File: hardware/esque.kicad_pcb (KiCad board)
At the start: 2 copper layers, 54.6 x 39.7 mm, 11 parts, among them J2 Conn_01x03_Pin, J3 Conn_01x04_Pin

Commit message: Update two-board hardware design to revision 0.9
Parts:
- removed A1: Arduino_Nano_v2.x, Module:Arduino_Nano
- removed J3: Conn_01x04_Pin, Connector:FanPinHeader_1x04_P2.54mm_Vertical
- added C1: 10pF, Capacitor_SMD:C_1206_3216Metric, B.Cu at (27.0, 40.0)
- added C2: 10pF, Capacitor_SMD:C_1206_3216Metric, B.Cu at (42.0, 36.5)
- added C3: 100nF, Capacitor_SMD:C_1206_3216Metric, B.Cu at (27.9, 30.2)
- added C4: 100nF, Capacitor_SMD:C_1206_3216Metric, B.Cu at (40.5, 31.5)
- added C6: 10uF 16V, Turbimeter:CP_Radial_D5_P2_SingleFace, F.Cu at (47.0, 38.5)
- added J1: SENSOR_LINK_2mm, Turbimeter:StackHeader_1x06_P2mm_Base_SingleFace, F.Cu at (47.3, 24.0)
- added J4: USB_STACK_4_1.27mm, Turbimeter:USB_StackHeader_2x02_P1.27mm_Base_v09, F.Cu at (33.5, 47.0)
- added R4: 10k, Resistor_SMD:R_1206_3216Metric, B.Cu at (45.5, 31.7)
- added U1: MCP6002-E/P, Turbimeter:MCP6002_DIP8_SingleFace, F.Cu at (30.5, 34.4)
- D1: value LED -> BPW34 scatter; footprint LED_THT:LED_D3.0mm_Horizontal_O6.35mm_Z10.0mm -> Turbimeter:BPW34_Holder_v08; moved to F.Cu
- D2: value LED -> BPW34 reference; footprint LED_THT:LED_D3.0mm_Horizontal_O6.35mm_Z10.0mm -> Turbimeter:BPW34_Holder_v08; moved to F.Cu
- D3: value LED -> 850 nm IR; footprint LED_THT:LED_D3.0mm_Horizontal_O6.35mm_Z10.0mm -> Turbimeter:LED850_LeadPads_P2.54mm; moved to F.Cu
- J2: value Conn_01x03_Pin -> USB2_CABLE_4_WIRES; footprint Connector_PinHeader_2.54mm:PinHeader_1x03_P2.54mm_Vertical -> Turbimeter:USB_Cable_WireHoles_2x02_P2mm; moved to F.Cu
- R1, R2: value R -> 1M; footprint Resistor_THT:R_Axial_DIN0207_L6.3mm_D2.5mm_P10.16mm_Horizontal -> Resistor_SMD:R_1206_3216Metric
- R3: value R -> 10k; footprint Resistor_THT:R_Axial_DIN0207_L6.3mm_D2.5mm_P10.16mm_Horizontal -> Resistor_SMD:R_1206_3216Metric
- R5, R6: value R -> 220R; footprint Resistor_THT:R_Axial_DIN0207_L6.3mm_D2.5mm_P10.16mm_Horizontal -> Resistor_SMD:R_1206_3216Metric
- moved R6 124.7 mm to (19.0, 29.0), turned to 90 degrees
- moved R5 116.0 mm to (19.0, 34.0)
- moved D2 104.8 mm to (23.0, 29.5), turned to -90 degrees
- moved D1 102.5 mm to (31.5, 30.2)
- moved J2 100.9 mm to (25.7, 43.5), turned to 0 degrees
- moved D3 99.2 mm to (23.5, 25.7), turned to 90 degrees
- moved R1 88.8 mm to (27.0, 35.0), turned to 90 degrees
- moved R2 73.6 mm to (42.0, 34.0)
- moved R3 72.3 mm to (44.5, 27.0), turned to 90 degrees
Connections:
- D1 pad 1: D5 -> /SCATTER_SUM
- D1 pad 2: Net-(D1-A) -> /GND
- D2 pad 1: D4 -> /REFERENCE_SUM
- D2 pad 2: Net-(D2-A) -> /GND
- D3 pad 1: D3 -> /GND
- D3 pad 2: Net-(D3-A) -> /LED_ANODE
- J2 pad 1: GND -> /USB_VBUS
- J2 pad 2: +5V -> /GND
- J2 pad 3: A1 -> /USB_DM
- R1 pad 1: Net-(D3-A) -> /SCATTER_OUT
- R1 pad 2: +3.3V -> /SCATTER_SUM
- R2 pad 1: Net-(D2-A) -> /REFERENCE_OUT
- R2 pad 2: +3.3V -> /REFERENCE_SUM
- R3 pad 1: Net-(D1-A) -> /3V3
- R3 pad 2: +3.3V -> /VREF
- R5 pad 1: A5 -> /LED_DRIVE
- R5 pad 2: +3.3V -> /LED_R1
- R6 pad 1: A4 -> /LED_R1
- R6 pad 2: +3.3V -> /LED_ANODE
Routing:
- net +3.3V: track 88.5 -> 0.00 mm
- net A4: track 43.0 -> 0.00 mm
- net A5: track 33.1 -> 0.00 mm
- net Net-(D1-A): track 28.0 -> 0.00 mm
- net Net-(D2-A): track 23.0 -> 0.00 mm
- net A1: track 18.7 -> 0.00 mm
- net Net-(D3-A): track 17.2 -> 0.00 mm
- net D3: track 13.7 -> 0.00 mm
- net D4: track 11.9 -> 0.00 mm
- net D5: track 11.4 -> 0.00 mm
- net +5V: track 4.38 -> 0.00 mm
- net GND: vias 4 -> 0
- removed copper zone on F.Cu, net GND
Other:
- board size 54.6 x 39.7 mm -> 37.1 x 35.6 mm
- board text added: "44mm circle = enclosure clearance; NOT Edge.Cuts"
- board text added: "B.Cu ONLY — SOLDER SIDE: SMD, ALL JOINTS AND ROUTING"
- board text added: "BOTTOM"
- board text added: "Design: Ing. Alex M. Rivera"
- board text added: "J1: GND / 3V3 / LED / SCATTER / REFERENCE / GND"
- board text added: "J2/J4/J5 USB 1..4: VBUS / GND / D- / D+; CC termination at cable plugs / OTG adapter"
- board text added: "NO F.Cu TRACKS / ZONES; NO VIAS. PAD 1 MARKED SQUARE."
- board text added: "SMD + ALL SOLDER + TRACKS"
- board text added: "THT TOP - SOLDER BELOW"
- board text added: "TOP"
- board text added: "TOP / F.Cu: THROUGH-HOLE COMPONENTS AND MALE HEADERS"
- board text added: "Turbidimeter | floor 1 - sensor / cable entry"
- board text added: "UNROUTED - DO NOT FABRICATE"

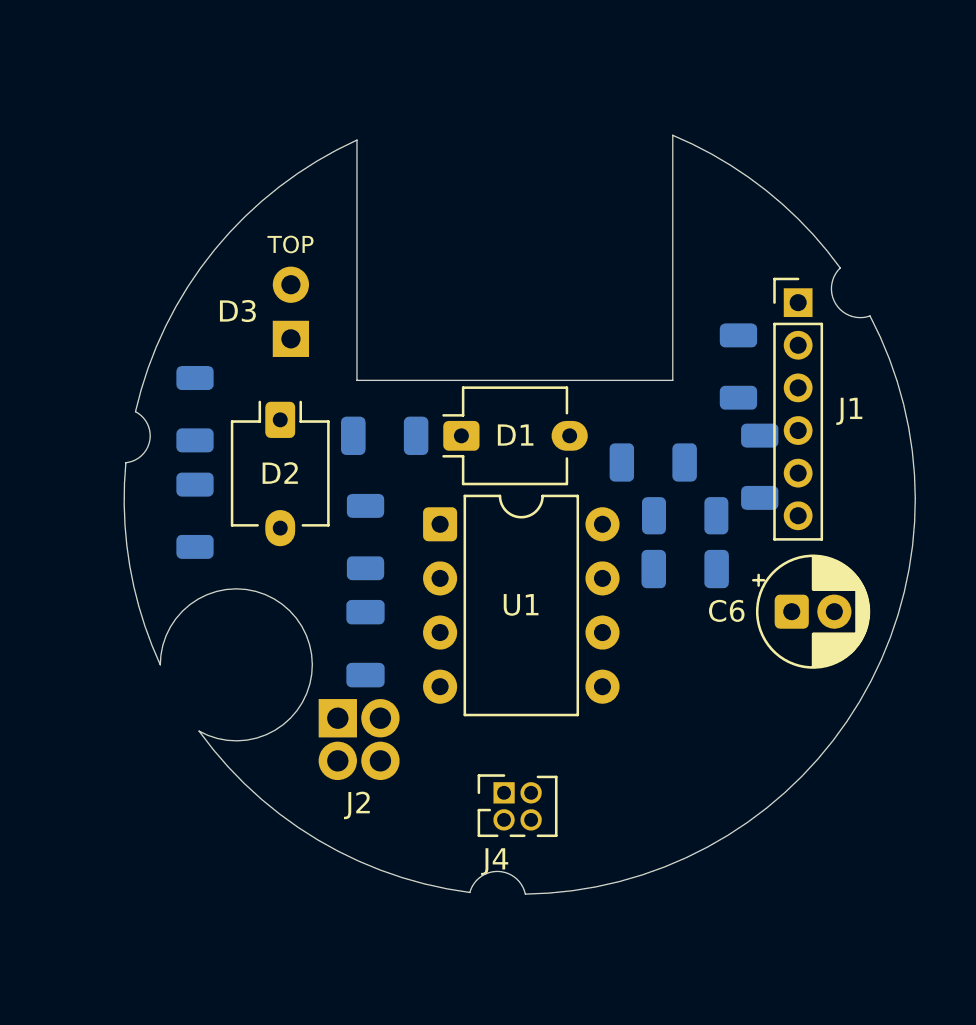
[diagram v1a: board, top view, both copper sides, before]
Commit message: Update 32 files (3D, docs, hardware, raíz)
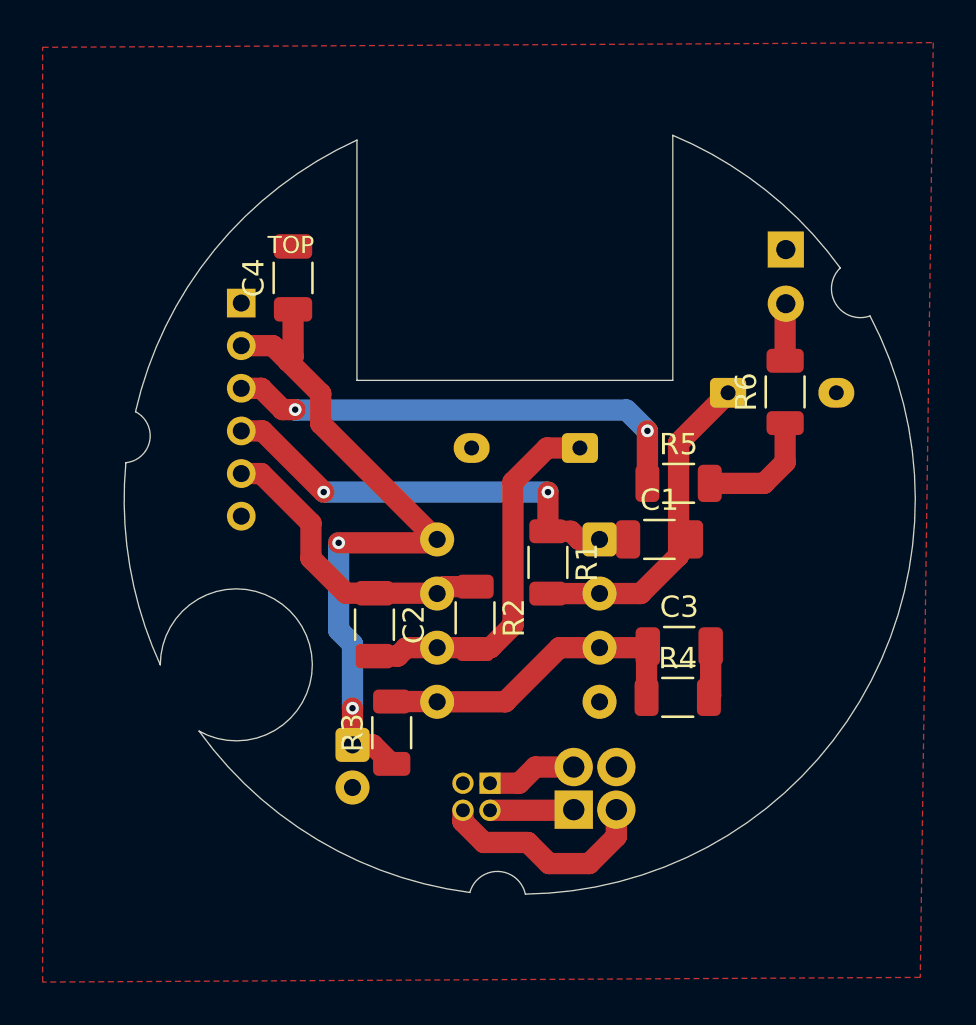
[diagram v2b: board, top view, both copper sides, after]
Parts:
- C1, C2, C3, C4, R1, R2, R3, R4, R5, R6: moved to F.Cu
- C6, D1, D2, D3, J1, J2, J4, U1: moved to B.Cu
- moved R6 27.7 mm to (46.7, 28.2)
- moved J1 26.1 mm to (21.2, 24.0), turned to 180 degrees
- moved R3 23.7 mm to (28.2, 44.2)
- moved D3 23.6 mm to (46.7, 21.5), turned to -90 degrees
- moved R5 22.7 mm to (41.7, 32.5), turned to 0 degrees
- moved C6 21.5 mm to (26.4, 44.8), turned to -90 degrees
- moved C4 19.0 mm to (23.6, 22.8), turned to 90 degrees
- moved C3 17.0 mm to (41.7, 40.1), turned to 0 degrees
- moved C2 14.8 mm to (27.4, 39.1), turned to -90 degrees
- moved C1 14.6 mm to (40.8, 35.1), turned to 0 degrees
- moved D2 14.1 mm to (37.1, 30.8), turned to 180 degrees
- moved D1 12.7 mm to (44.0, 28.2)
- moved J2 11.9 mm to (36.8, 47.8)
- moved R4 11.5 mm to (41.6, 42.5), turned to 0 degrees
- moved R2 11.0 mm to (32.1, 38.8), turned to -90 degrees
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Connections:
- J2 pad 1: /USB_VBUS -> /USB_DM
- J2 pad 2: /GND -> /USB_DP
- J2 pad 3: /USB_DM -> /USB_VBUS
- J2 pad 4: /USB_DP -> /GND
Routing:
- net /3V3: track 0.00 -> 33.0 mm, vias 0 -> 2
- net /LED_DRIVE: track 0.00 -> 22.3 mm, vias 0 -> 2
- net /SCATTER_OUT: track 0.00 -> 21.3 mm, vias 0 -> 2
- net /REFERENCE_SUM: track 0.00 -> 17.6 mm
- net /SCATTER_SUM: track 0.00 -> 16.1 mm
- net /VREF: track 0.00 -> 15.5 mm
- net /REFERENCE_OUT: track 0.00 -> 14.4 mm
- net /USB_DP: track 0.00 -> 10.3 mm
- net /LED_R1: track 0.00 -> 5.79 mm
- net /USB_VBUS: track 0.00 -> 4.24 mm
- net /USB_DM: track 0.00 -> 3.94 mm
- net /LED_ANODE: track 0.00 -> 2.69 mm
- net /GND: track 0.00 -> 2.42 mm
- added copper zone on F.Cu, net /GND

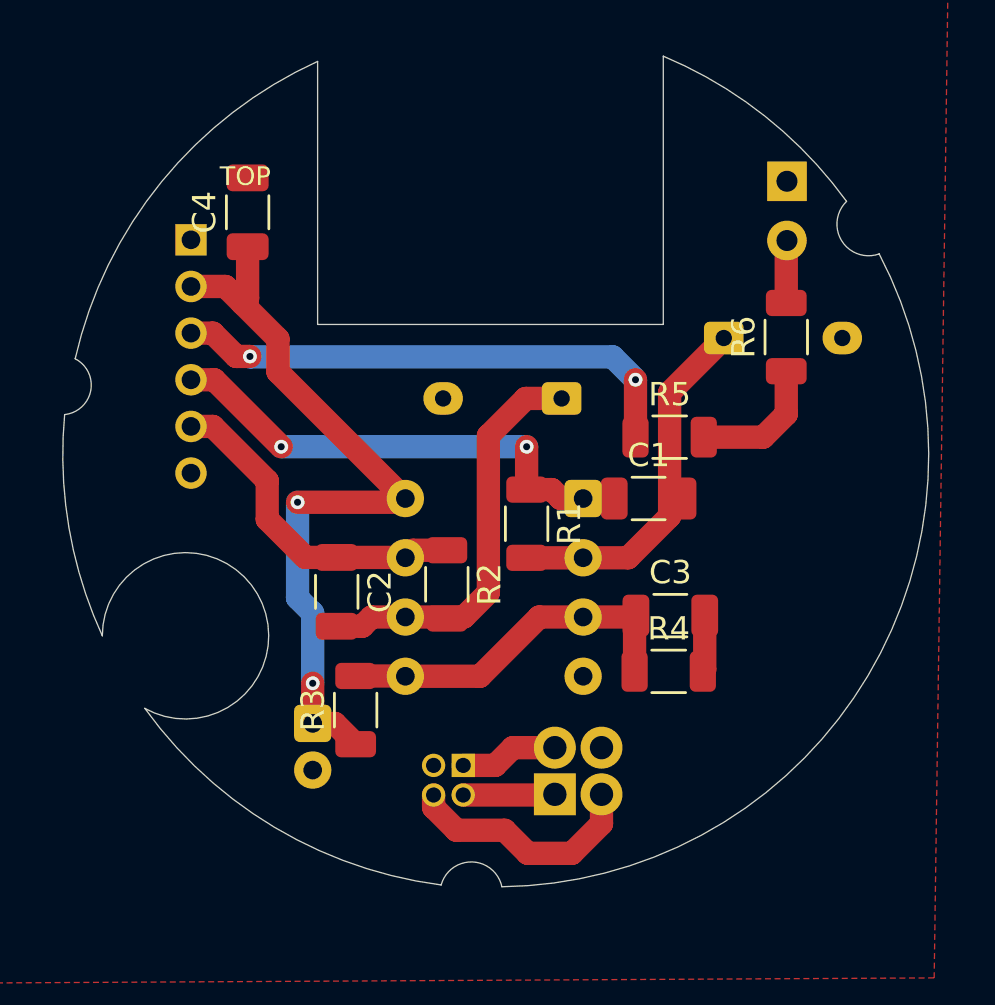
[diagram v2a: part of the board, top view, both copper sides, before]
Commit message: Organize project, add calibration app and record prototype bench results
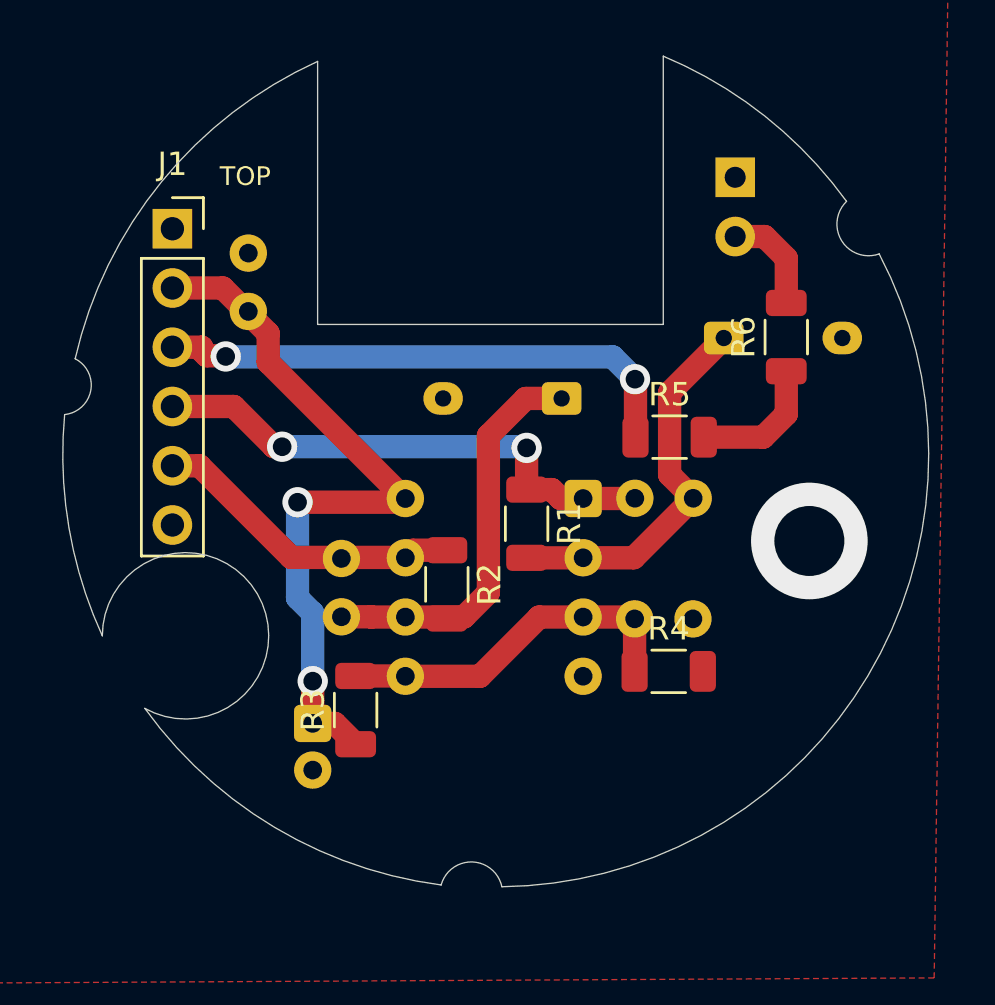
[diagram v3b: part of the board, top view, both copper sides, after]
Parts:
- removed J2: USB2_CABLE_4_WIRES, Turbimeter:USB_Cable_WireHoles_2x02_P2mm
- removed J4: USB_STACK_4_1.27mm, Turbimeter:USB_StackHeader_2x02_P1.27mm_Base_v09
- C1, C2, C3, C4: footprint Capacitor_SMD:C_1206_3216Metric -> Capacitor_THT:C_Disc_D5.0mm_W2.5mm_P2.50mm; moved to B.Cu
- J1: footprint Turbimeter:StackHeader_1x06_P2mm_Base_SingleFace -> Connector_PinSocket_2.54mm:PinSocket_1x06_P2.54mm_Vertical; moved to F.Cu
- moved C4 4.25 mm to (23.6, 27.1)
- moved D3 2.23 mm to (44.5, 21.3)
- moved C3 1.54 mm to (40.2, 40.3)
- moved C2 1.44 mm to (27.6, 37.7)
- moved J1 0.93 mm to (20.4, 23.5), turned to 0 degrees
- moved C1 0.59 mm to (40.2, 35.1)
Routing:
- net /USB_DP: track 10.3 -> 0.00 mm
- net /USB_VBUS: track 4.24 -> 0.00 mm
- net /USB_DM: track 3.94 -> 0.00 mm
- net /GND: track 2.42 -> 0.00 mm, vias 0 -> 1
- net /3V3: track 33.0 -> 31.1 mm
- net /LED_ANODE: track 2.69 -> 4.49 mm
- net /SCATTER_OUT: track 21.3 -> 22.5 mm
- net /REFERENCE_OUT: track 14.4 -> 13.5 mm
- net /LED_DRIVE: track 22.3 -> 23.0 mm
